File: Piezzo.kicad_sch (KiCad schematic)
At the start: 0 parts

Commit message: added piezzo circuit and i2c line
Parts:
- added LS1: ~, dz_mech:PT-1140PEQ, symbol #dzdb:s_misc/MALL-539-PT-1140PEQ
- added Q3: 50V, dz_dio:onsemi_Mosfet_BSS138, symbol #dzdb:s_misc/ONSE-BSS138
- added R38: 1k, Resistor_SMD:R_0603_1608Metric, symbol #dzdb:g_res/R-1k-0603
- added R39: 0, Resistor_SMD:R_0603_1608Metric, symbol #dzdb:g_res/R-0-0603
- added R40: 100, Resistor_SMD:R_0402_1005Metric, symbol #dzdb:g_res/R-100-0402
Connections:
- new net: LS1.1 (+), R38.1, R39.2
- new net: LS1.2 (-), Q3.3, R38.2
- new net: Q3.1, R40.2
- new net 10V: R39.1
- new net GND: Q3.2
- new net Piezo_ctrl: R40.1
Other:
- note added: "Optimally replace the 1k with a fast switching diode."
- note added: "This 0R is a placeholder. Apply different resistors to get different volumes"

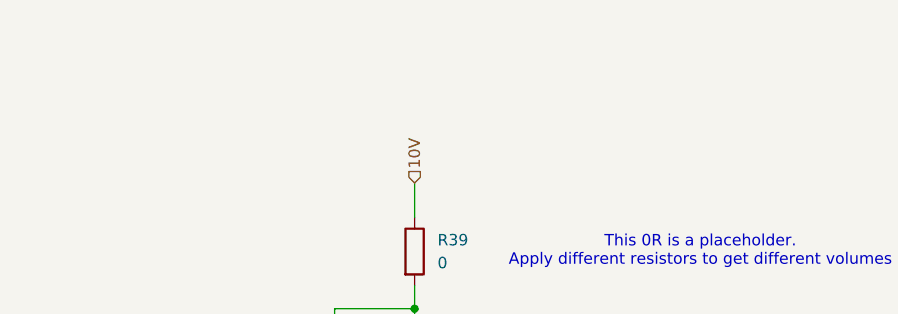
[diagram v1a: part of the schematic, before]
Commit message: chore: added a comment that piezzo buzzer wont be implemented right now
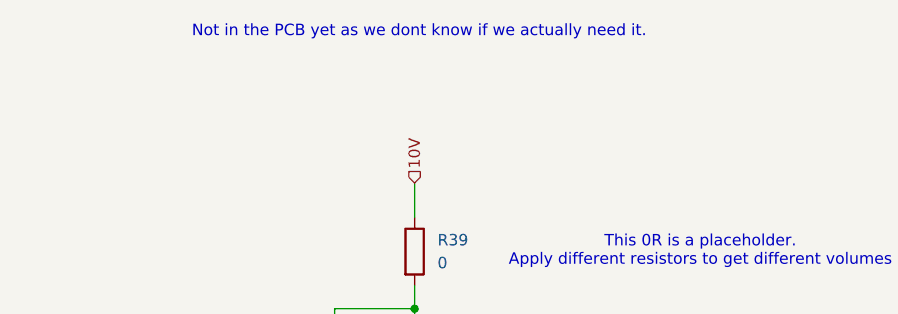
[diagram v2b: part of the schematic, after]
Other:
- note added: "Not in the PCB yet as we dont know if we actually need it."
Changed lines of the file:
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@@
+		)
+	)
+	(text "Not in the PCB yet as we dont know if we actually need it."
+		(exclude_from_sim no)
+		(at 173.228 49.276 0)
+		(effects
+			(font
+				(size 1.27 1.27)
+			)
 		)
 	)

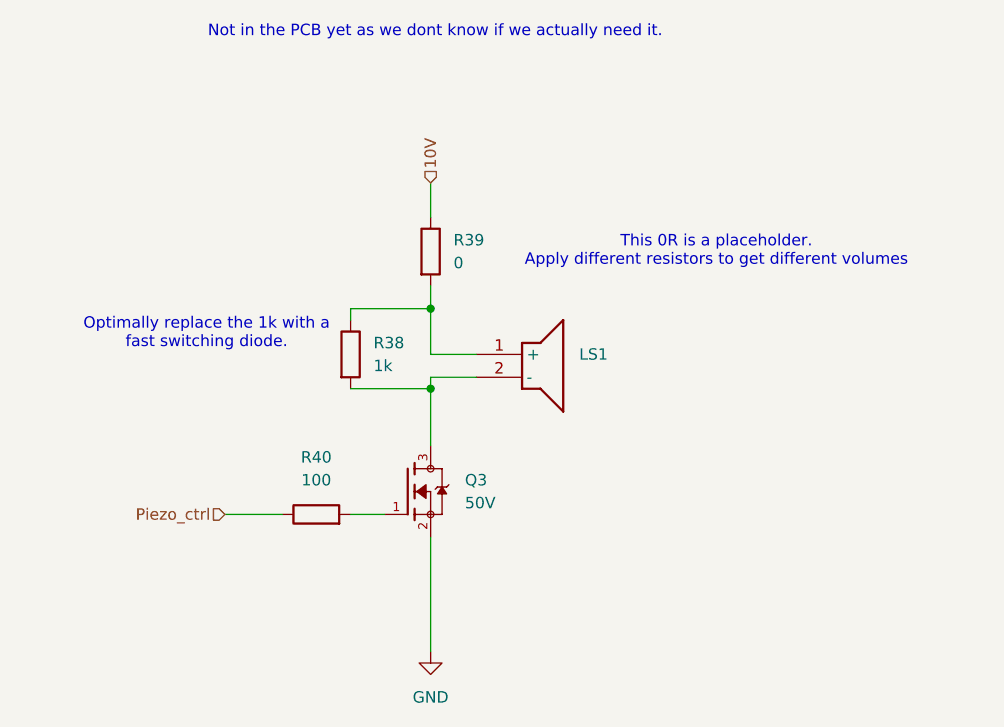
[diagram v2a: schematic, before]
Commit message: changed the piezzo buzzer
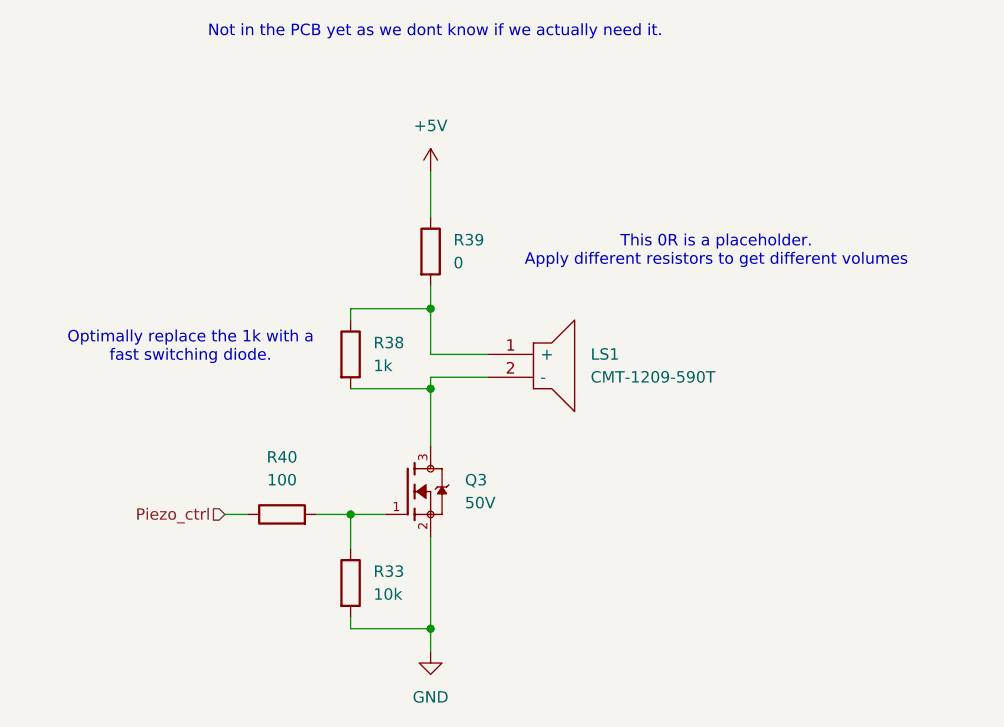
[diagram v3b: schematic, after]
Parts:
- removed LS1: ~, dz_mech:PT-1140PEQ, symbol #dzdb:s_misc/MALL-539-PT-1140PEQ
- added LS1: Piezo Buzzers & Audio Indicators 12mmx9mm deep Ma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, dz_mech:CMT1209590T, symbol #dzdb:s_mech/M-SAMESKY-CMT-1209-590T
- added R33: 10k, Resistor_SMD:R_0603_1608Metric, symbol #dzdb:g_res/R-10k-0603
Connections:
- net GND: now also R33.2
- net at R38.1, R39.2: now also LS1.1 (+)
- net at Q3.3, R38.2: now also LS1.2 (-)
- net at Q3.1, R40.2: now also R33.1
- net 10V renamed +5V
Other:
- moved on the sheet: R40

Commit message: added the diode
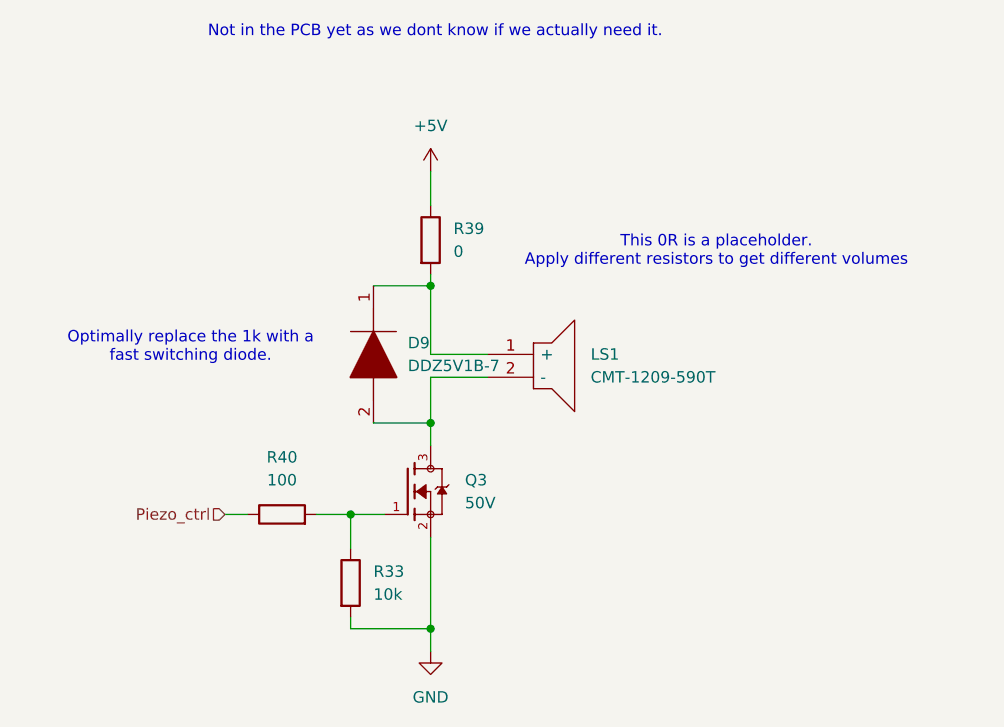
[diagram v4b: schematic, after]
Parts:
- removed R38: 1k, Resistor_SMD:R_0603_1608Metric, symbol #dzdb:g_res/R-1k-0603
- added D9: DDZ5V1B-7, dz_dio:SOD3716X145N, symbol #dzdb:s_dio/D-DIO-DDZ5V1B-7
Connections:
- net at LS1.1 (+), R39.2: now also D9.1
- net at LS1.2 (-), Q3.3: now also D9.2
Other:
- moved on the sheet: R39

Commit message: chore: more cleanup
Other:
- company: (none) -> Evan
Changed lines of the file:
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@@
 	(generator_version "9.0")
 	(paper "A4")
+	(title_block
+		(date "2025-11-18")
+		(company "Evan")
+	)
 	(text "Optimally replace the 1k with a\nfast switching diode. \n"
 		(exclude_from_sim no)

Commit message: chore: Loads of redoing stuff. Added a Changelog
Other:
- title: (none) -> Nautilus_Mainboard
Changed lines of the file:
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@@
 	(paper "A4")
 	(title_block
+		(title "Nautilus_Mainboard")
 		(date "2025-11-19")
 		(rev "0")

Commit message: chore: replaced 0 ohm with jumpers (not complete)
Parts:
- removed R39: 0, Resistor_SMD:R_0603_1608Metric, symbol #dzdb:g_res/R-0-0603
- added JP18: -, Jumper:SolderJumper-2_P1.3mm_Open_RoundedPad1.0x1.5mm, symbol #dzdb:g_mech/Jumper-2P1.3mm_Rounded
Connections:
- net +5V: now also JP18.2 (B)
- net at D9.1, LS1.1 (+): now also JP18.1 (A)
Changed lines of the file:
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@@
+	)
+	(symbol
+		(lib_id "#dzdb:g_mech/Jumper-2P1.3mm_Rounded")
+		(at 172.72 72.39 90)
+		(unit 1)
+		(exclude_from_sim no)
+		(in_bom no)
+		(on_board yes)
+		(dnp no)
+		(property "Reference" "JP18"
+			(at 169.164 72.39 90)
+			(effects
+				(font
+					(size 1.27 1.27)
+				)
+			)
+		)
+		(property "Value" "-"
+			(at 170.688 73.406 90)
+			(effects
+				(font
+					(size 1.27 1.27)
+				)
+			)
+		)
+		(property "Footprint" "Jumper:SolderJumper-2_P1.3mm_Open_RoundedPad1.0x1.5mm"
+			(at 172.72 72.39 0)
+			(effects
+				(font
+					(size 1.27 1.27)
+				)
+				(hide yes)
+			)
+		)
+		(property "Datasheet" "~"
+			(at 172.72 72.39 0)
+			(effects
+				(font
+					(size 1.27 1.27)
+				)
+				(hide yes)
+			)
+		)
+		(property "Description" "Solder Jumper"
+			(at 172.72 72.39 0)
+			(effects
+				(font
+					(size 1.27 1.27)
+				)
+				(hide yes)
+			)
+		)
+		(property "IPN" "Jumper-2P1.3mm_Rounded"
+			(at 172.72 72.39 0)
+			(effects
+				(font
+					(size 1.27 1.27)
+				)
+				(hide yes)
+			)
+		)
+		(property "Comments" "Rounded Jumper Pads 1.0x1.5mm"
+			(at 172.72 72.39 0)
+			(effects
+				(font
+					(size 1.27 1.27)
+				)
+				(hide yes)
+			)
+		)
+		(pin "2"
+		)
+		(pin "1"
+		)
+		(instances
+			(project "nautilus_mainboard"
+				(path "/ce1819b2-f280-40ed-834f-6fe4d12f809d/7439593a-de4f-4d56-b463-481360a4f617"
+					(reference "JP18")
+					(unit 1)
+				)
+			)
+		)
 	)
 	(symbol
@@
 					(unit 1)
 				)
-			)
-		)
-	)
-	(symbol
-		(lib_id "#dzdb:g_res/R-0-0603")
-		(at 172.72 72.39 0)
-		(unit 1)
-		(exclude_from_sim no)
-		(in_bom yes)
-		(on_board yes)
-		(dnp no)
-		(fields_autoplaced yes)
-		(property "Reference" "R39"
-			(at 175.26 71.1199 0)
-			(effects
-				(font
-					(size 1.27 1.27)
-				)
-				(justify left)
-			)
-		)
-		(property "Value" "0"
-			(at 175.26 73.6599 0)
-			(effects
-				(font
-					(size 1.27 1.27)
-				)
-				(justify left)
-			)
-		)
-		(property "Footprint" "Resistor_SMD:R_0603_1608Metric"
-			(at 170.942 72.39 90)
-			(effects
-				(font
-					(size 1.27 1.27)
-				)
-				(hide yes)
-			)
-		)
-		(property "Datasheet" "https://www.we-online.com/components/products/datasheet/560112116001.pdf"
-			(at 172.72 72.39 0)
-			(effects
-				(font
-					(size 1.27 1.27)
-				)
-				(hide yes)
-			)
-		)
-		(property "Description" "Thick Film Resistors - SMD WRIS-RSKS <0.05 Ohms  0.1 W Jumper 0603"
-			(at 172.72 72.39 0)
-			(effects
-				(font
-					(size 1.27 1.27)
-				)
-				(hide yes)
-			)
-		)
-		(property "IPN" "R-0-0603"
-			(at 172.72 72.39 0)
-			(effects
-				(font
-					(size 1.27 1.27)
-				)
-				(hide yes)
-			)
-		)
-		(property "MPN" "560112116001"
-			(at 172.72 72.39 0)
-			(effects
-				(font
-					(size 1.27 1.27)
-				)
-				(hide yes)
-			)
-		)
-		(property "Manufacturer" "Wurth Elektronik"
-			(at 172.72 72.39 0)
-			(effects
-				(font
-					(size 1.27 1.27)
-				)
-				(hide yes)
-			)
-		)
-		(property "Resistance" "0"
-			(at 172.72 72.39 0)
-			(effects
-				(font
-					(size 1.27 1.27)
-				)
-				(hide yes)
-			)
-		)
-		(property "Power" "0.1W"
-			(at 172.72 72.39 0)
-			(effects
-				(font
-					(size 1.27 1.27)
-				)
-				(hide yes)
-			)
-		)
-		(property "Material" "Thick film"
-			(at 172.72 72.39 0)
-			(effects
-				(font
-					(size 1.27 1.27)
-				)
-				(hide yes)
-			)
-		)
-		(property "Tolerance" "5%"
-			(at 172.72 72.39 0)
-			(effects
-				(font
-					(size 1.27 1.27)
-				)
-				(hide yes)
-			)
-		)
-		(property "Supplier" "Mouser"
-			(at 172.72 72.39 0)
-			(effects
-				(font
-					(size 1.27 1.27)
-				)
-				(hide yes)
-			)
-		)
-		(property "SPN" "710-560112116001"
-			(at 172.72 72.39 0)
-			(effects
-				(font
-					(size 1.27 1.27)
-				)
-				(hide yes)
-			)
-		)
-		(property "LCSC" "CXXXXX"
-			(at 172.72 72.39 0)
-			(effects
-				(font
-					(size 1.27 1.27)
-				)
-				(hide yes)
-			)
-		)
-		(property "Comment" "lifecycle=Active; note=Auto-generated"
-			(at 172.72 72.39 0)
-			(effects
-				(font
-					(size 1.27 1.27)
-				)
-				(hide yes)
-			)
-		)
-		(pin "2"
-		)
-		(pin "1"
-		)
-		(instances
-			(project "nautilus_mainboard"
-				(path "/ce1819b2-f280-40ed-834f-6fe4d12f809d/7439593a-de4f-4d56-b463-481360a4f617"
-					(reference "R39")
-					(unit 1)
-				)
